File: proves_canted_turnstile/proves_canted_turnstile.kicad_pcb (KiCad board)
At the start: 4 copper layers, 100 x 100 mm, 26 parts, among them J1 Conn_Coaxial, J2 Conn_02x02_Counter_Clockwise, U1 QBA-07+, U2 QBA-07+, U3 QBA-07+

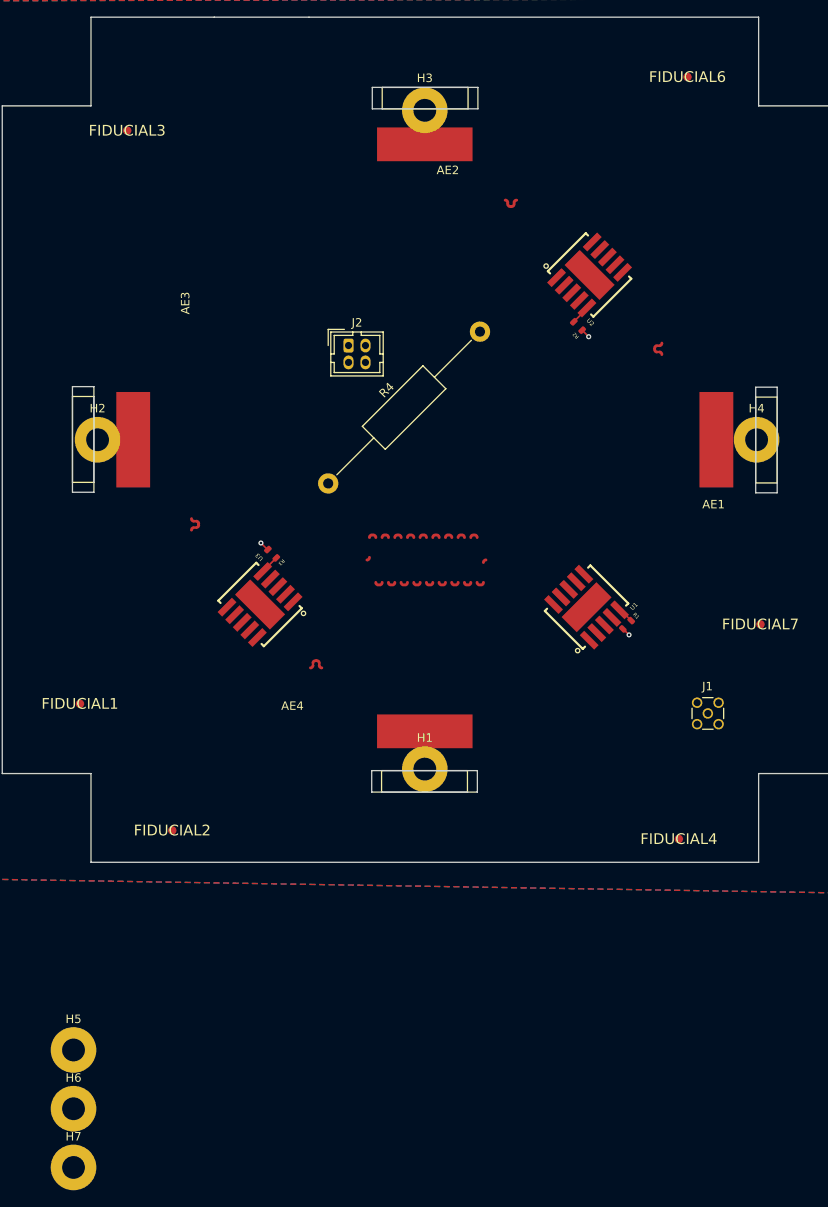
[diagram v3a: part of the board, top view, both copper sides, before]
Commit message: updated pad positions for antenna elements
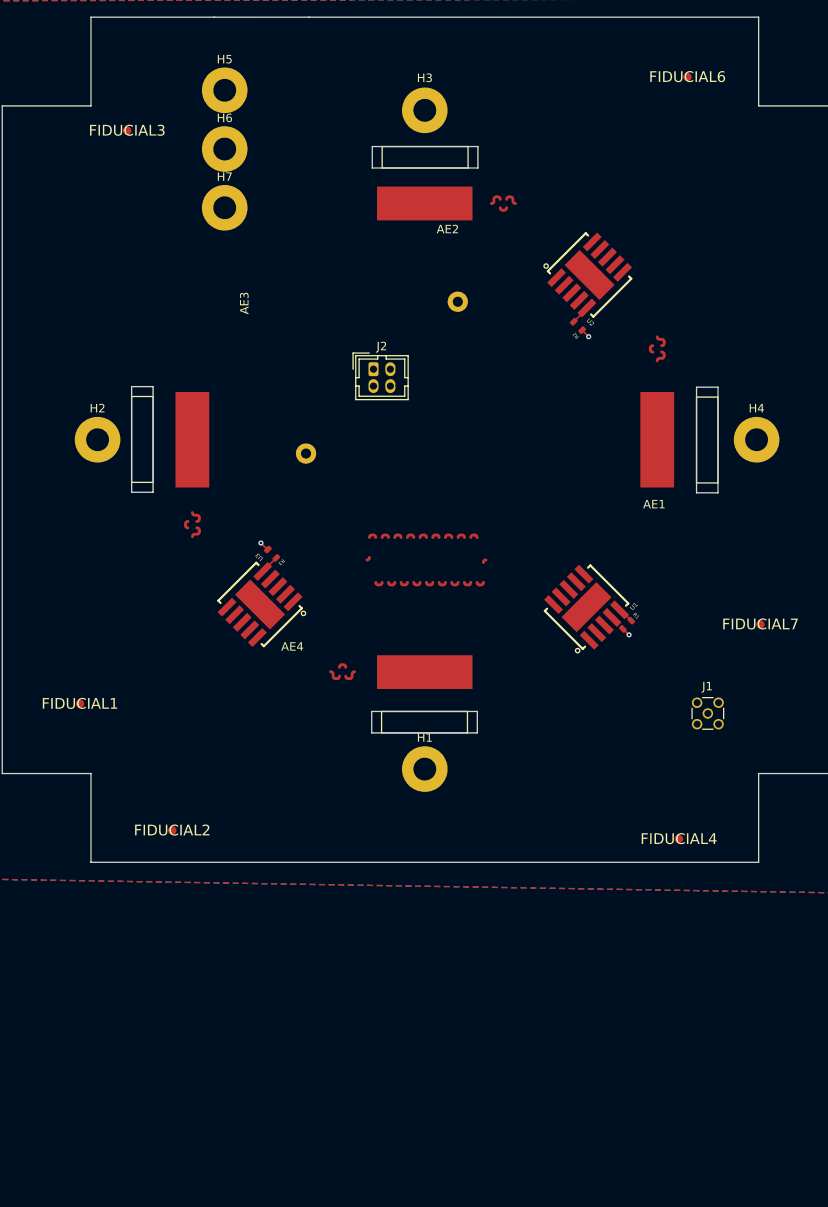
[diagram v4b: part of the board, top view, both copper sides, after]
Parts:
- R4: moved to B.Cu
- moved H7 115.0 mm to (120.0, 55.1)
- moved H5 115.0 mm to (120.0, 41.2)
- moved H6 115.0 mm to (120.0, 48.1)
- moved AE1 7.00 mm to (171.2, 82.5)
- moved AE2 7.00 mm to (143.7, 55.0)
- moved AE3 7.00 mm to (116.2, 82.5)
- moved AE4 7.00 mm to (143.7, 110.0)
- moved R4 4.41 mm to (129.6, 84.2)
- moved J2 4.07 mm to (137.6, 74.2)

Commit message: porting proves features
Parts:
- removed H5, H6, H7: MountingHole, MountingHole:MountingHole_2.7mm_M2.5_Pad
- removed J2: Conn_02x02_Counter_Clockwise, Connector_Hirose:Hirose_DF11-4DP-2DSA_2x02_P2.00mm_Vertical
- added G***: LOGO, LOGO, B.Cu at (167.6, 36.8)
- added J10: WDT Disable Jumper, Connector_PinHeader_2.54mm:PinHeader_1x02_P2.54mm_Vertical, B.Cu at (118.9, 44.4)
- added J11: DEBUG, Connector_Hirose:Hirose_DF11-12DP-2DSA_2x06_P2.00mm_Vertical, F.Cu at (125.0, 62.6)
- added J12: USB_C_Receptacle_USB2.0_16P, Connector_USB:USB_C_Receptacle_HRO_TYPE-C-31-M-12, B.Cu at (98.8, 61.6)
- added J3: Battery Charge Bypass, Connector_PinHeader_2.54mm:PinHeader_1x02_P2.54mm_Vertical, B.Cu at (121.5, 49.8)
- added J6: FC Reset Jumper, Connector_PinHeader_2.54mm:PinHeader_1x02_P2.54mm_Vertical, B.Cu at (118.9, 35.2)
- added J7: FC USB Bootselect Jumper, Connector_PinHeader_2.54mm:PinHeader_1x02_P2.54mm_Vertical, B.Cu at (118.9, 39.8)
- added J8: USB_C_Receptacle_USB2.0_16P, Connector_USB:USB_C_Receptacle_HRO_TYPE-C-31-M-12, B.Cu at (98.8, 50.6)
- added J9: DF11-4DP-2DSA, Connector_Hirose:Hirose_DF11-4DP-2DSA_2x02_P2.00mm_Vertical, F.Cu at (106.2, 51.8)
- added R26: 5.1k, Resistor_SMD:R_0603_1608Metric, B.Cu at (106.2, 63.8)
- added R27: 5.1k, Resistor_SMD:R_0603_1608Metric, B.Cu at (106.4, 59.8)
- added R5: 5.1k, Resistor_SMD:R_0603_1608Metric, B.Cu at (107.2, 53.2)
- added R6: 5.1k, Resistor_SMD:R_0603_1608Metric, B.Cu at (106.8, 48.0)
- moved R1 1.46 mm to (168.8, 103.6), turned to -135 degrees
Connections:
- R4 pad 1: Net-(J2-Pin_3) -> BURN
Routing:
- net GND: track 3.27 -> 77.3 mm, vias 3 -> 202
- net /Payload_VBUS: track 0.00 -> 7.25 mm
- net /Payload_D-: track 0.00 -> 6.54 mm
- net /Payload_D+: track 0.00 -> 6.37 mm
- net Net-(J8-CC1): track 0.00 -> 4.11 mm
- net Net-(J8-CC2): track 0.00 -> 3.51 mm
- net USB_D+: track 0.00 -> 2.99 mm
- net USB_D-: track 0.00 -> 2.99 mm
- net Net-(J12-CC1): track 0.00 -> 2.95 mm
- net Net-(J12-CC2): track 0.00 -> 2.78 mm
- added copper zone on B.Cu, net (none)
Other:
- board text added: "BRONCO SPACE Educational Product For Instructional Use Only"

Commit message: Finished board
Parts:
- added G***: LOGO, LOGO, B.Cu at (169.2, 50.0)
- added G***: LOGO, LOGO, B.Cu at (135.2, 79.0)
- added G***: LOGO, LOGO, B.Cu at (180.4, 54.6)
- added G***: LOGO, LOGO, B.Cu at (113.5, 125.4)
- added G***: LOGO, LOGO, B.Cu at (157.1, 59.9)
- added G***: LOGO, LOGO, B.Cu at (163.7, 55.6)
- added G***: LOGO, LOGO, B.Cu at (169.4, 59.6)
- added G***: LOGO, LOGO, B.Cu at (157.7, 51.0)
- added G***: LOGO, LOGO, B.Cu at (127.2, 125.2)
- R4: footprint Resistor_THT:R_Axial_DIN0411_L9.9mm_D3.6mm_P25.40mm_Horizontal -> Resistor_THT:R_Axial_DIN0309_L9.0mm_D3.2mm_P12.70mm_Horizontal
- moved FIDUCIAL4 81.0 mm to (183.9, 49.4)
- moved R4 18.4 mm to (146.3, 76.5), turned to -135 degrees
- moved J11 10.2 mm to (115.0, 60.6), turned to 0 degrees
- moved J6 3.04 mm to (121.4, 36.9), turned to 90 degrees
- moved FIDUCIAL2 2.88 mm to (113.7, 125.9)
- moved J7 2.67 mm to (121.4, 40.7), turned to 90 degrees
- moved J9 2.61 mm to (108.8, 51.6)
- moved J10 2.54 mm to (121.4, 44.4), turned to 90 degrees
- moved R5 1.84 mm to (105.8, 52.0)
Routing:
- net BURN: track 0.00 -> 35.1 mm
- net ~{FC_RESET}: track 0.00 -> 31.1 mm
- net USB_D-: track 2.99 -> 27.6 mm, vias 0 -> 2
- net FC_USBBOOT: track 0.00 -> 23.9 mm
- net USB_D+: track 2.99 -> 26.3 mm, vias 0 -> 2
- net WDT_DISABLE: track 0.00 -> 19.4 mm
- net Dir_Chrg_In: track 0.00 -> 13.9 mm
- net /Payload_VBUS: track 7.25 -> 17.7 mm
- net /Payload_D+: track 6.37 -> 11.9 mm
- net /Payload_D-: track 6.54 -> 11.4 mm, vias 0 -> 2
- net Net-(J8-CC1): track 4.11 -> 2.22 mm
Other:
- board text added: "+"
- board text added: "-"
- board text added: "3PySquared Antenna Board V3 Pragun Bethapudi | Michael Pham Nicole Maggard | Ernesto Montes"
- board text added: "Ad Astra Tempore"
- board text added: "BOOT SELECT"
- board text added: "Batt Charging Bypass"
- board text added: "Circle is Ground"
- board text added: "FC Jumpers"
- board text added: "RESET"
- board text added: "THE PLEIADES FIVE"
- board text added: "The PROVES Kit V3"
- board text added: "WDT DISABLE"

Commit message: adjusted antenna landing pads
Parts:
- J9: moved to B.Cu
- moved J9 2.62 mm to (110.6, 49.7), turned to -90 degrees
- moved R6 2.47 mm to (107.7, 45.7)
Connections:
- net /Payload_VBUS renamed Payload_VBUS
- J8 pad A6: /Payload_D+ -> Payload_D+
- J8 pad A7: /Payload_D- -> Payload_D-
- J8 pad B6: /Payload_D+ -> Payload_D+
- J8 pad B7: /Payload_D- -> Payload_D-
- J9 pad 1: /Payload_D- -> Payload_D+
- J9 pad 3: /Payload_D+ -> Payload_D-
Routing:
- net Payload_D-: track 0.00 -> 13.2 mm, vias 0 -> 2
- net Payload_D+: track 0.00 -> 13.2 mm
- net /Payload_D+: track 11.9 -> 0.00 mm
- net /Payload_D-: track 11.4 -> 0.00 mm, vias 2 -> 0
- net Net-(J8-CC2): track 3.51 -> 0.00 mm
- net GND: track 76.9 -> 73.9 mm, vias 202 -> 199
- net Payload_VBUS: track 17.7 -> 18.8 mm

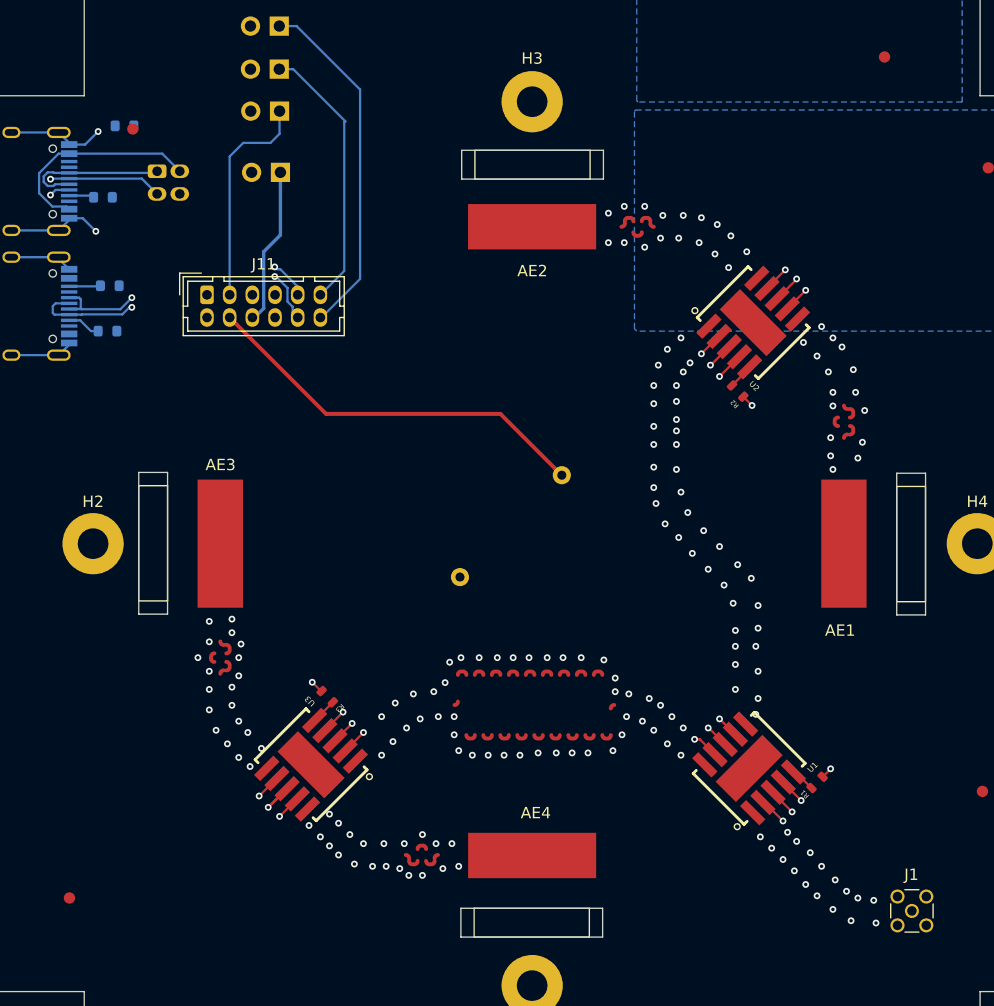
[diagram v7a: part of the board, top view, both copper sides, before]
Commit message: adjusted traces and updates
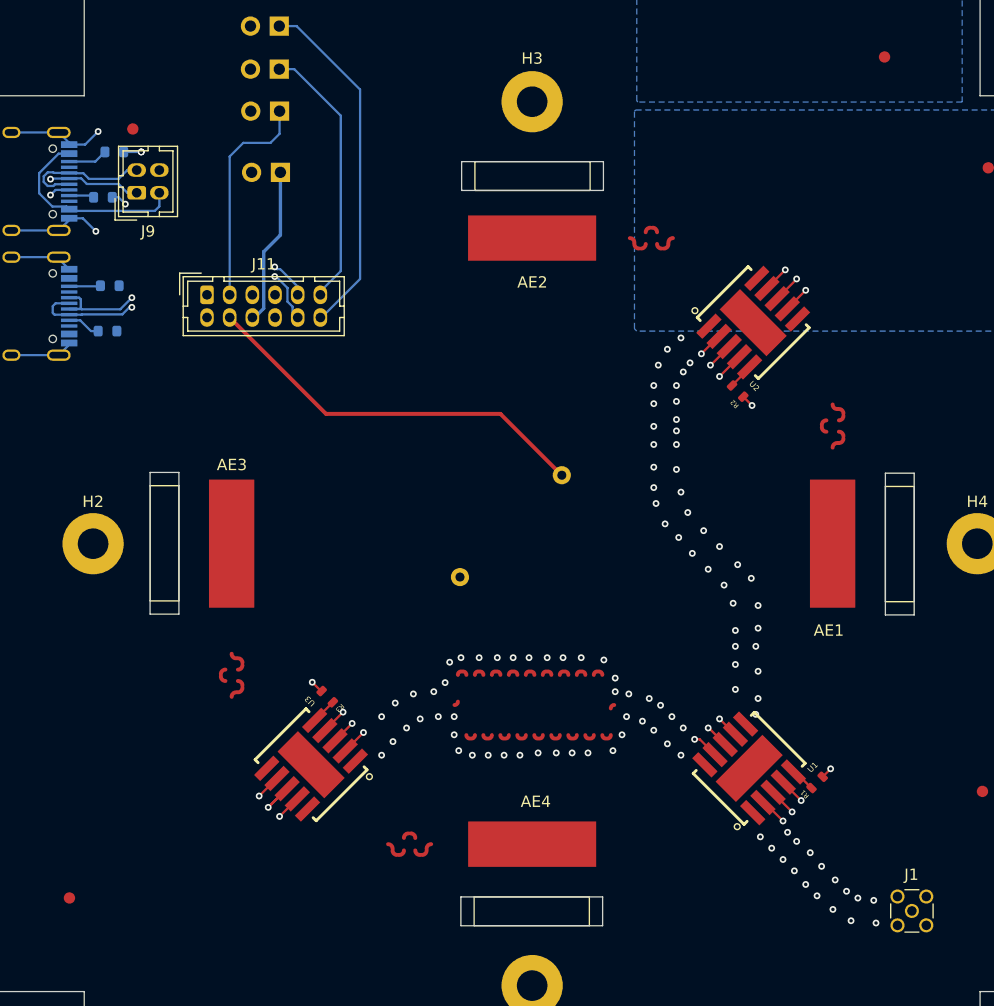
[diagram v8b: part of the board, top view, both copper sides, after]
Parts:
- J9: moved to F.Cu
- moved J9 2.62 mm to (108.8, 51.6), turned to 90 degrees
- moved R6 2.47 mm to (106.8, 48.0)
- moved AE1 1.00 mm to (170.2, 82.5)
- moved AE2 1.00 mm to (143.7, 56.0)
- moved AE3 1.00 mm to (117.2, 82.5)
- moved AE4 1.00 mm to (143.7, 109.0)
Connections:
- net Payload_VBUS renamed /Payload_VBUS
- J8 pad A6: Payload_D+ -> /Payload_D+
- J8 pad A7: Payload_D- -> /Payload_D-
- J8 pad B6: Payload_D+ -> /Payload_D+
- J8 pad B7: Payload_D- -> /Payload_D-
- J9 pad 1: Payload_D+ -> /Payload_D-
- J9 pad 3: Payload_D- -> /Payload_D+
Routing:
- net Payload_D-: track 13.2 -> 0.00 mm, vias 2 -> 0
- net Payload_D+: track 13.2 -> 0.00 mm
- net /Payload_D+: track 0.00 -> 11.9 mm
- net /Payload_D-: track 0.00 -> 11.4 mm, vias 0 -> 2
- net Net-(J8-CC2): track 0.00 -> 3.51 mm
- net GND: track 73.9 -> 76.9 mm, vias 199 -> 128
- net /Payload_VBUS: track 18.8 -> 17.7 mm
